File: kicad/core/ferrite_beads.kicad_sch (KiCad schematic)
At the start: 5 parts

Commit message: created new component based on simulation and replace resistive model with inductive model
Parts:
- MCE00: renamed from FB00; value FB_00 -> MCE; footprint Inductor_SMD:L_1206_3216Metric -> (none); symbol core_memory:CoreBead_3W -> core_memory:MCE; now left out of the parts list
- MCE01: renamed from FB01; value FB_01 -> MCE; footprint Inductor_SMD:L_1206_3216Metric -> (none); symbol core_memory:CoreBead_3W -> core_memory:MCE; now left out of the parts list
- MCE10: renamed from FB10; value FB_10 -> MCE; footprint Inductor_SMD:L_1206_3216Metric -> (none); symbol core_memory:CoreBead_3W -> core_memory:MCE; now left out of the parts list
- MCE11: renamed from FB11; value FB_11 -> MCE; footprint Inductor_SMD:L_1206_3216Metric -> (none); symbol core_memory:CoreBead_3W -> core_memory:MCE; now left out of the parts list
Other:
- note added: "MAGNETIC CORES — 2×2 MCE XA→XB top→bottom; YA→YB right→left Sense: LL→UR diagonal (MCE10/MCE01 mirrored about Y), center tap, then LR→UL"
- note removed: "FERRITE BEADS — 2×2 stand-in XA→XB top→bottom; YA→YB right→left Sense: LL→UR diagonal (FB10/FB01 mirrored about Y), center tap, then LR→UL"
- title: Ferrite Beads -> Magnetic Cores
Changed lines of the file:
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@@
 	(paper "A3")
 	(title_block
-		(title "Ferrite Beads")
-		(comment 1 "2x2 CoreBead; X top/bot Y L/R S diagonal; FB01/FB10 mirror Y")
-	)
-	(text "FERRITE BEADS — 2×2 stand-in\nXA→XB top→bottom; YA→YB right→left\nSense: LL→UR diagonal (FB10/FB01 mirrored about Y), center tap, then LR→UL"
+		(title "Magnetic Cores")
+		(comment 1 "2x2 MCE; X top/bot Y L/R S diagonal; MCE01/MCE10 mirror Y")
+	)
+	(text "MAGNETIC CORES — 2×2 MCE\nXA→XB top→bottom; YA→YB right→left\nSense: LL→UR diagonal (MCE10/MCE01 mirrored about Y), center tap, then LR→UL"
 		(exclude_from_sim no)
 		(at 20 15 0)
@@
 	)
 	(symbol
-		(lib_id "core_memory:CoreBead_3W")
+		(lib_id "core_memory:MCE")
 		(at 100.33 54.61 0)
 		(unit 1)
 		(body_style 1)
 		(exclude_from_sim no)
-		(in_bom yes)
-		(on_board yes)
-		(in_pos_files yes)
+		(in_bom no)
+		(on_board no)
+		(in_pos_files no)
 		(dnp no)
-		(property "Reference" "FB00"
+		(property "Reference" "MCE00"
 			(at 102.87 41.91 0)
 			(show_name no)
@@
 			)
 		)
-		(property "Value" "FB_00"
+		(property "Value" "MCE"
 			(at 102.87 44.45 0)
 			(show_name no)
@@
 			)
 		)
-		(property "Footprint" "Inductor_SMD:L_1206_3216Metric"
+		(property "Footprint" ""
 			(at 100.33 54.61 0)
 			(hide yes)
@@
 				(justify left)
 			)
+		)
+		(property "Sim.Device" "SUBCKT"
+			(at 0 0 0)
+			(hide yes)
+			(show_name no)
+			(do_not_autoplace no)
+			(effects (font (size 1.27 1.27)) (justify left))
+		)
+		(property "Sim.Name" "mce"
+			(at 0 0 0)
+			(hide yes)
+			(show_name no)
+			(do_not_autoplace no)
+			(effects (font (size 1.27 1.27)) (justify left))
+		)
+		(property "Sim.Library" "../core_element_sim/models/coremem.cir"
+			(at 0 0 0)
+			(hide yes)
+			(show_name no)
+			(do_not_autoplace no)
+			(effects (font (size 1.27 1.27)) (justify left))
+		)
+		(property "Sim.Pins" "1=X1 2=X2 3=Y1 4=Y2 5=S1 6=S2"
+			(at 0 0 0)
+			(hide yes)
+			(show_name no)
+			(do_not_autoplace no)
+			(effects (font (size 1.27 1.27)) (justify left))
 		)
 		(pin "1"
@@
 			(project "core"
 				(path "/fabf9ba2-76e6-4325-a1a0-bc01b9516551/a1b2c3d4-e5f6-4789-a012-bbbbbbbbbbbb"
-					(reference "FB00")
+					(reference "MCE00")
 					(unit 1)
 				)
@@
 	)
 	(symbol
-		(lib_id "core_memory:CoreBead_3W")
+		(lib_id "core_memory:MCE")
 		(at 161.29 105.41 0)
 		(unit 1)
 		(body_style 1)
 		(exclude_from_sim no)
-		(in_bom yes)
-		(on_board yes)
-		(in_pos_files yes)
+		(in_bom no)
+		(on_board no)
+		(in_pos_files no)
 		(dnp no)
-		(property "Reference" "FB11"
+		(property "Reference" "MCE11"
 			(at 163.83 92.71 0)
 			(show_name no)
@@
 			)
 		)
-		(property "Value" "FB_11"
+		(property "Value" "MCE"
 			(at 163.83 95.25 0)
 			(show_name no)
@@
 			)
 		)
-		(property "Footprint" "Inductor_SMD:L_1206_3216Metric"
+		(property "Footprint" ""
 			(at 161.29 105.41 0)
 			(hide yes)
@@
 				(justify left)
 			)
+		)
+		(property "Sim.Device" "SUBCKT"
+			(at 0 0 0)
+			(hide yes)
+			(show_name no)
+			(do_not_autoplace no)
+			(effects (font (size 1.27 1.27)) (justify left))
+		)
+		(property "Sim.Name" "mce"
+			(at 0 0 0)
+			(hide yes)
+			(show_name no)
+			(do_not_autoplace no)
+			(effects (font (size 1.27 1.27)) (justify left))
+		)
+		(property "Sim.Library" "../core_element_sim/models/coremem.cir"
+			(at 0 0 0)
+			(hide yes)
+			(show_name no)
+			(do_not_autoplace no)
+			(effects (font (size 1.27 1.27)) (justify left))
+		)
+		(property "Sim.Pins" "1=X1 2=X2 3=Y1 4=Y2 5=S1 6=S2"
+			(at 0 0 0)
+			(hide yes)
+			(show_name no)
+			(do_not_autoplace no)
+			(effects (font (size 1.27 1.27)) (justify left))
 		)
 		(pin "1"
@@
 			(project "core"
 				(path "/fabf9ba2-76e6-4325-a1a0-bc01b9516551/a1b2c3d4-e5f6-4789-a012-bbbbbbbbbbbb"
-					(reference "FB11")
+					(reference "MCE11")
 					(unit 1)
 				)
@@
 	)
 	(symbol
-		(lib_id "core_memory:CoreBead_3W")
+		(lib_id "core_memory:MCE")
 		(at 161.29 54.61 0)
 		(mirror y)
@@
 		(body_style 1)
 		(exclude_from_sim no)
-		(in_bom yes)
-		(on_board yes)
-		(in_pos_files yes)
+		(in_bom no)
+		(on_board no)
+		(in_pos_files no)
 		(dnp no)
-		(property "Reference" "FB01"
+		(property "Reference" "MCE01"
 			(at 163.83 41.91 0)
 			(show_name no)
@@
 			)
 		)
-		(property "Value" "FB_01"
+		(property "Value" "MCE"
 			(at 163.83 44.45 0)
 			(show_name no)
@@
 			)
 		)
-		(property "Footprint" "Inductor_SMD:L_1206_3216Metric"
+		(property "Footprint" ""
 			(at 161.29 54.61 0)
 			(hide yes)
@@
 				(justify left)
 			)
+		)
+		(property "Sim.Device" "SUBCKT"
+			(at 0 0 0)
+			(hide yes)
+			(show_name no)
+			(do_not_autoplace no)
+			(effects (font (size 1.27 1.27)) (justify left))
+		)
+		(property "Sim.Name" "mce"
+			(at 0 0 0)
+			(hide yes)
+			(show_name no)
+			(do_not_autoplace no)
+			(effects (font (size 1.27 1.27)) (justify left))
+		)
+		(property "Sim.Library" "../core_element_sim/models/coremem.cir"
+			(at 0 0 0)
+			(hide yes)
+			(show_name no)
+			(do_not_autoplace no)
+			(effects (font (size 1.27 1.27)) (justify left))
+		)
+		(property "Sim.Pins" "1=X1 2=X2 3=Y1 4=Y2 5=S1 6=S2"
+			(at 0 0 0)
+			(hide yes)
+			(show_name no)
+			(do_not_autoplace no)
+			(effects (font (size 1.27 1.27)) (justify left))
 		)
 		(pin "1"
@@
 			(project "core"
 				(path "/fabf9ba2-76e6-4325-a1a0-bc01b9516551/a1b2c3d4-e5f6-4789-a012-bbbbbbbbbbbb"
-					(reference "FB01")
+					(reference "MCE01")
 					(unit 1)
 				)
@@
 	)
 	(symbol
-		(lib_id "core_memory:CoreBead_3W")
+		(lib_id "core_memory:MCE")
 		(at 99.06 105.41 0)
 		(mirror y)
@@
 		(body_style 1)
 		(exclude_from_sim no)
-		(in_bom yes)
-		(on_board yes)
-		(in_pos_files yes)
+		(in_bom no)
+		(on_board no)
+		(in_pos_files no)
 		(dnp no)
-		(property "Reference" "FB10"
+		(property "Reference" "MCE10"
 			(at 101.6 92.71 0)
 			(show_name no)
@@
 			)
 		)
-		(property "Value" "FB_10"
+		(property "Value" "MCE"
 			(at 101.6 95.25 0)
 			(show_name no)
@@
 			)
 		)
-		(property "Footprint" "Inductor_SMD:L_1206_3216Metric"
+		(property "Footprint" ""
 			(at 99.06 105.41 0)
 			(hide yes)
@@
 				(justify left)
 			)
+		)
+		(property "Sim.Device" "SUBCKT"
+			(at 0 0 0)
+			(hide yes)
+			(show_name no)
+			(do_not_autoplace no)
+			(effects (font (size 1.27 1.27)) (justify left))
+		)
+		(property "Sim.Name" "mce"
+			(at 0 0 0)
+			(hide yes)
+			(show_name no)
+			(do_not_autoplace no)
+			(effects (font (size 1.27 1.27)) (justify left))
+		)
+		(property "Sim.Library" "../core_element_sim/models/coremem.cir"
+			(at 0 0 0)
+			(hide yes)
+			(show_name no)
+			(do_not_autoplace no)
+			(effects (font (size 1.27 1.27)) (justify left))
+		)
+		(property "Sim.Pins" "1=X1 2=X2 3=Y1 4=Y2 5=S1 6=S2"
+			(at 0 0 0)
+			(hide yes)
+			(show_name no)
+			(do_not_autoplace no)
+			(effects (font (size 1.27 1.27)) (justify left))
 		)
 		(pin "1"
@@
 			(project "core"
 				(path "/fabf9ba2-76e6-4325-a1a0-bc01b9516551/a1b2c3d4-e5f6-4789-a012-bbbbbbbbbbbb"
-					(reference "FB10")
+					(reference "MCE10")
 					(unit 1)
 				)

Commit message: Docs updated to match physical core layout.
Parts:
- added R2: DNP, Resistor_SMD:R_0805_2012Metric, symbol Device:R
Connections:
- net YA65: now also MCE00.6 (S2), R2.1
- net YB66: now also R2.2
- net YA66 renamed SENSE_FOLD
- net SENSE_FOLD: now also MCE10.6 (S2), R1.1
- removed net YB65: MCE00.6 (S2), MCE10.6 (S2), R1.1
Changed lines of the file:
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@@
 	(title_block
 		(title "Magnetic Cores")
-		(comment 1 "2x2 MCE; X top/bot Y L/R S diagonal; MCE01/MCE10 mirror Y")
+		(comment 1 "2x2 MCE; X/Y address weave; sense loops YA65-YA66 and YB65-YB66; center tap YA66=YB65")
 	)
 	(text "MAGNETIC CORES — 2×2 MCE\nXA→XB top→bottom; YA→YB right→left\nSense: LL→UR diagonal (MCE10/MCE01 mirrored about Y), center tap, then LR→UL"
@@
 	(wire
 		(pts
-			(xy 107.95 49.53) (xy 140.97 49.53)
+			(xy 107.95 49.53) (xy 120.65 49.53)
 		)
 		(stroke
@@
 	(wire
 		(pts
-			(xy 140.97 49.53) (xy 140.97 138.43)
+			(xy 153.67 110.49) (xy 153.67 138.43)
 		)
 		(stroke
@@
 		)
 	)
-	(label "YA65"
-		(at 143.51 114.3 0)
+	(hierarchical_label "YA65"
+		(shape passive)
+		(at 120.65 49.53 0)
 		(effects
 			(font
@@
 		)
 	)
-	(label "YB66"
+	(hierarchical_label "YB66"
+		(shape passive)
 		(at 81.28 90.17 180)
 		(effects
@@
 		)
 	)
-	(hierarchical_label "YB65"
-		(shape passive)
+	(label "YB65"
 		(at 87.63 100.33 180)
 		(effects
@@
 		)
 	)
+	(symbol
+		(lib_id "Device:R")
+		(at 210 160 0)
+		(unit 1)
+		(body_style 1)
+		(exclude_from_sim yes)
+		(in_bom no)
+		(on_board no)
+		(in_pos_files no)
+		(dnp yes)
+		(property "Reference" "R2"
+			(at 212.54 155.5 0)
+			(show_name no)
+			(do_not_autoplace no)
+			(effects
+				(font
+					(size 1.27 1.27)
+				)
+				(justify left)
+			)
+		)
+		(property "Value" "DNP"
+			(at 212.54 157.8 0)
+			(show_name no)
+			(do_not_autoplace no)
+			(effects
+				(font
+					(size 1.27 1.27)
+				)
+				(justify left)
+			)
+		)
+		(property "Footprint" "Resistor_SMD:R_0805_2012Metric"
+			(at 210 160 0)
+			(hide yes)
+			(show_name no)
+			(do_not_autoplace no)
+			(effects
+				(font
+					(size 1.27 1.27)
+				)
+				(justify left)
+			)
+		)
+		(property "Datasheet" ""
+			(at 210 160 0)
+			(hide yes)
+			(show_name no)
+			(do_not_autoplace no)
+			(effects
+				(font
+					(size 1.27 1.27)
+				)
+				(justify left)
+			)
+		)
+		(property "Description" ""
+			(at 210 160 0)
+			(hide yes)
+			(show_name no)
+			(do_not_autoplace no)
+			(effects
+				(font
+					(size 1.27 1.27)
+				)
+				(justify left)
+			)
+		)
+		(pin "1"
+		)
+		(pin "2"
+		)
+		(instances
+			(project "core"
+				(path "/fabf9ba2-76e6-4325-a1a0-bc01b9516551/a1b2c3d4-e5f6-4789-a012-bbbbbbbbbbbb"
+					(reference "R2")
+					(unit 1)
+				)
+			)
+		)
+	)
+	(wire
+		(pts
+			(xy 210 156.19) (xy 210 151.13)
+		)
+		(stroke
+			(width 0)
+			(type default)
+		)
+	)
+	(wire
+		(pts
+			(xy 210 163.81) (xy 210 168.91)
+		)
+		(stroke
+			(width 0)
+			(type default)
+		)
+	)
+	(label "YA65"
+		(at 210 151.13 0)
+		(effects
+			(font
+				(size 1.27 1.27)
+			)
+			(justify left)
+		)
+	)
+	(label "YB66"
+		(at 210 168.91 0)
+		(effects
+			(font
+				(size 1.27 1.27)
+			)
+			(justify left)
+		)
+	)

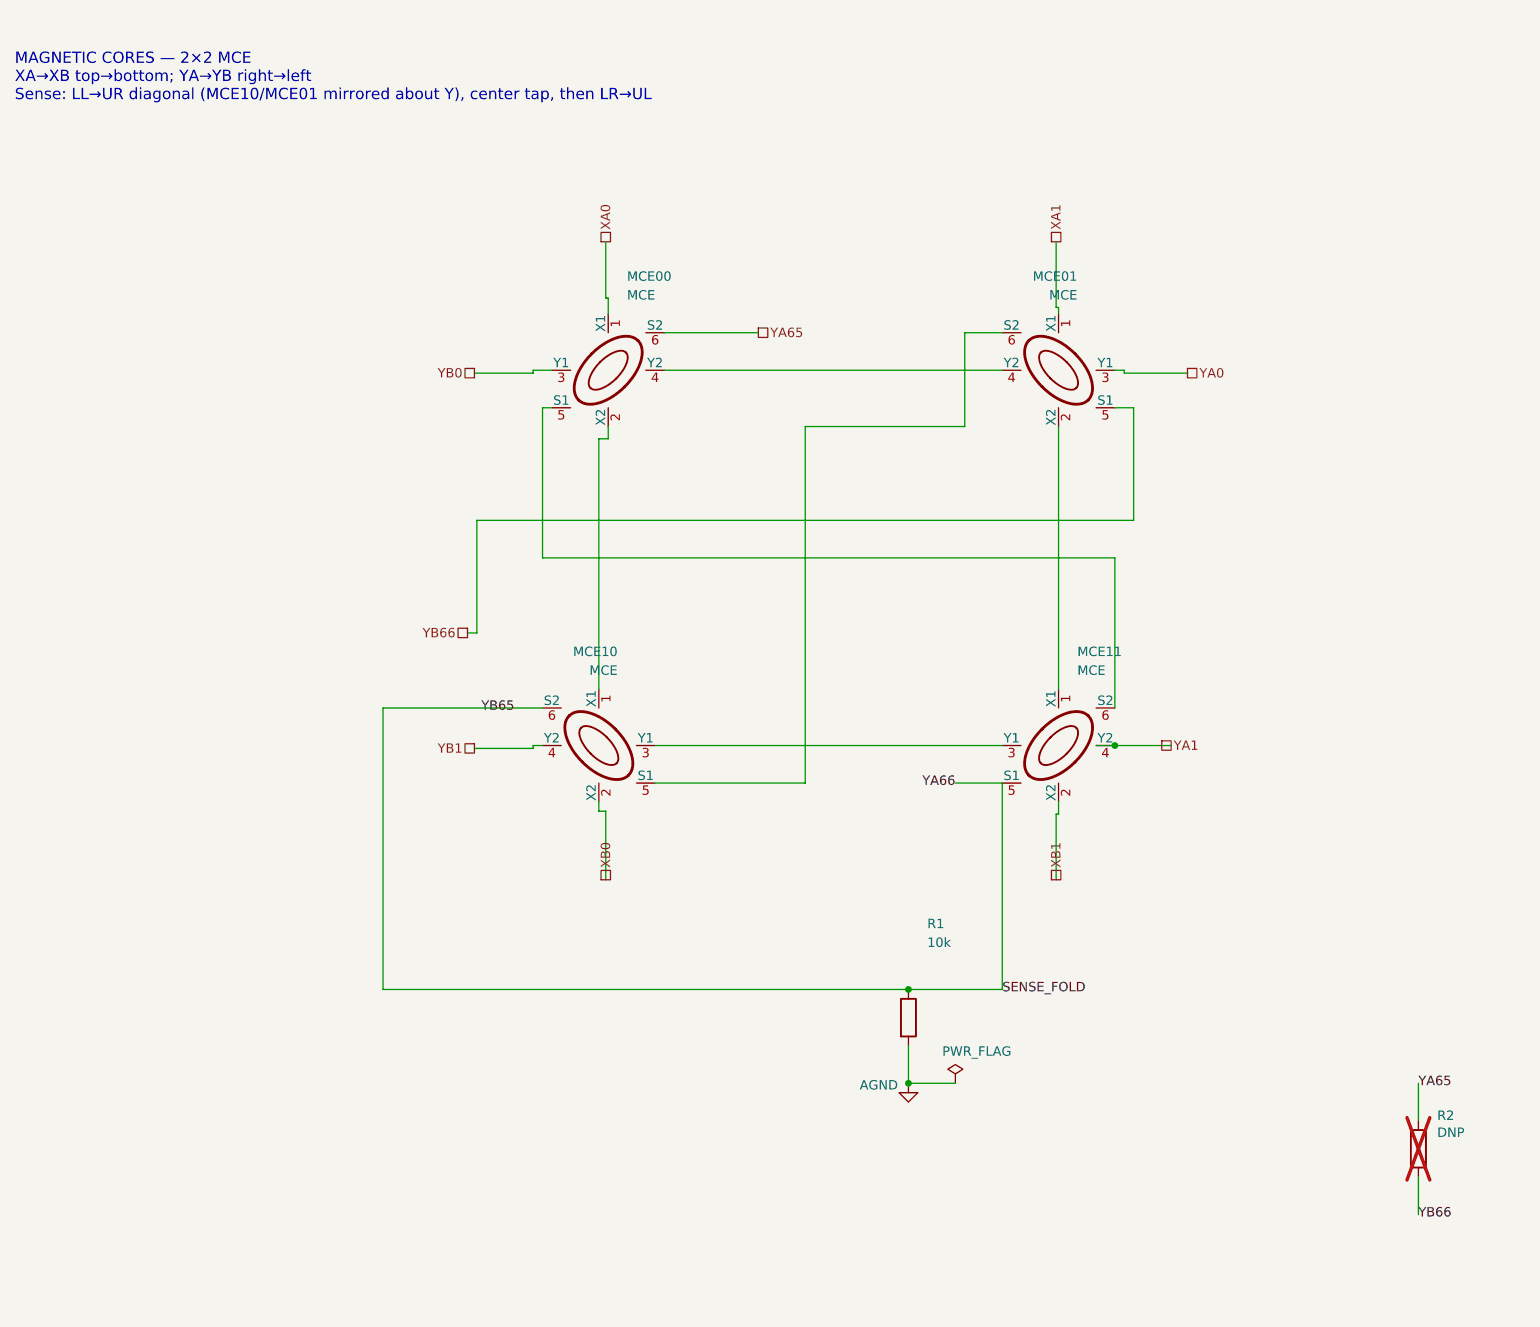
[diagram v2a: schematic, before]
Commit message: Prove the 2×2 access cycle from the address pins through decode, drive, and the sense latch.
Three current sinks, the diode matrix, and drive groups 0--7 are on the schematic. The four-core decks are the gate; weave inductance is still an open input.
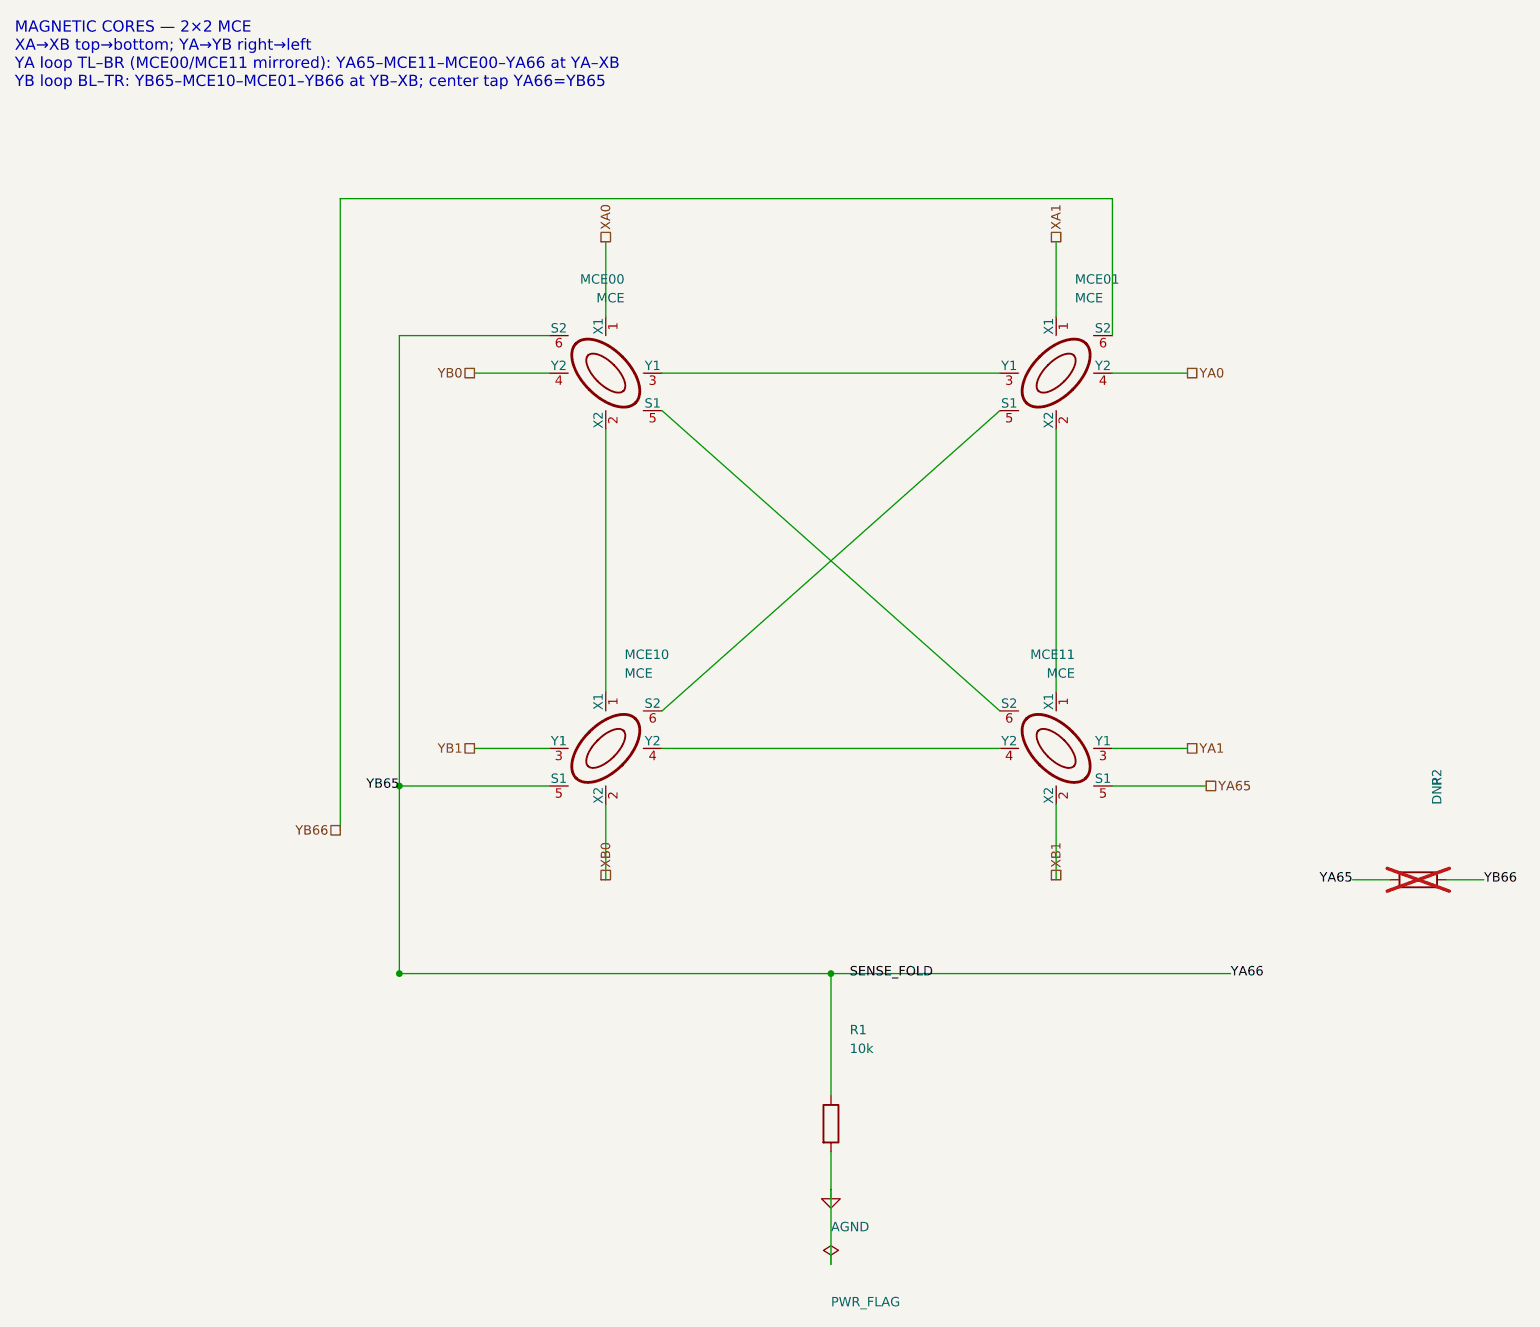
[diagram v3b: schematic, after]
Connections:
- net SENSE_FOLD: now also MCE00.6 (S2), MCE10.5 (S1); no longer MCE10.6 (S2), MCE11.5 (S1)
- net YA0: now also MCE01.4 (Y2); no longer MCE01.3 (Y1)
- net YA1: now also MCE11.3 (Y1); no longer MCE11.4 (Y2)
- net YA65: now also MCE11.5 (S1); no longer MCE00.6 (S2)
- net YB0: now also MCE00.4 (Y2); no longer MCE00.3 (Y1)
- net YB1: now also MCE10.3 (Y1); no longer MCE10.4 (Y2)
- net YB66: now also MCE01.6 (S2); no longer MCE01.5 (S1)
- new net: MCE10.4 (Y2), MCE11.4 (Y2)
- new net: MCE01.5 (S1), MCE10.6 (S2)
- new net: MCE00.3 (Y1), MCE01.3 (Y1)
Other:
- note added: "MAGNETIC CORES — 2×2 MCE XA→XB top→bottom; YA→YB right→left YA loop TL–BR (MCE00/MCE11 mirrored): YA65–MCE11–MCE00–YA66 at YA–XB YB loop BL–TR: YB65–MCE10–MCE01–YB66 at YB–XB; center tap YA66=YB65"
- note removed: "MAGNETIC CORES — 2×2 MCE XA→XB top→bottom; YA→YB right→left Sense: LL→UR diagonal (MCE10/MCE01 mirrored about Y), center tap, then LR→UL"
